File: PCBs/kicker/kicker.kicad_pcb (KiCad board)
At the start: 2 copper layers, 11 parts, among them Q1 CSD19534Q5A

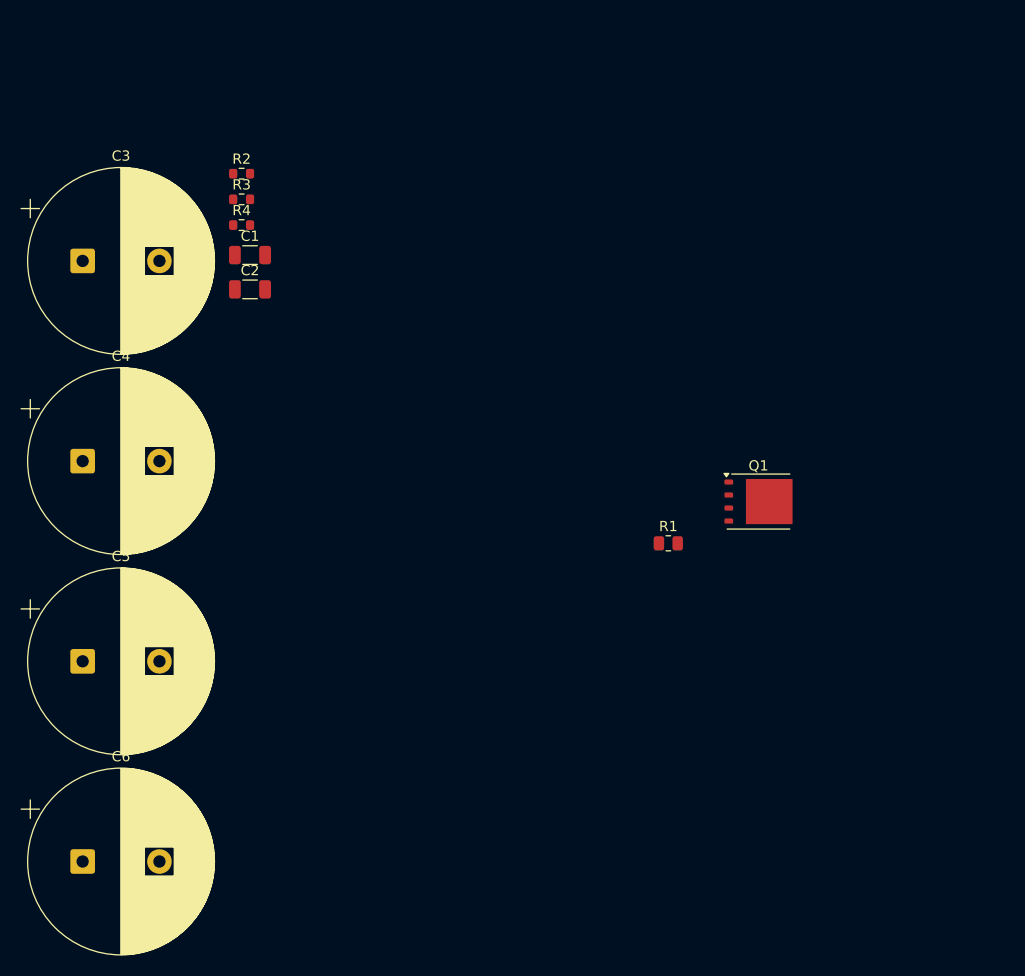
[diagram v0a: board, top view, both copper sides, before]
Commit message: fix driver footprint
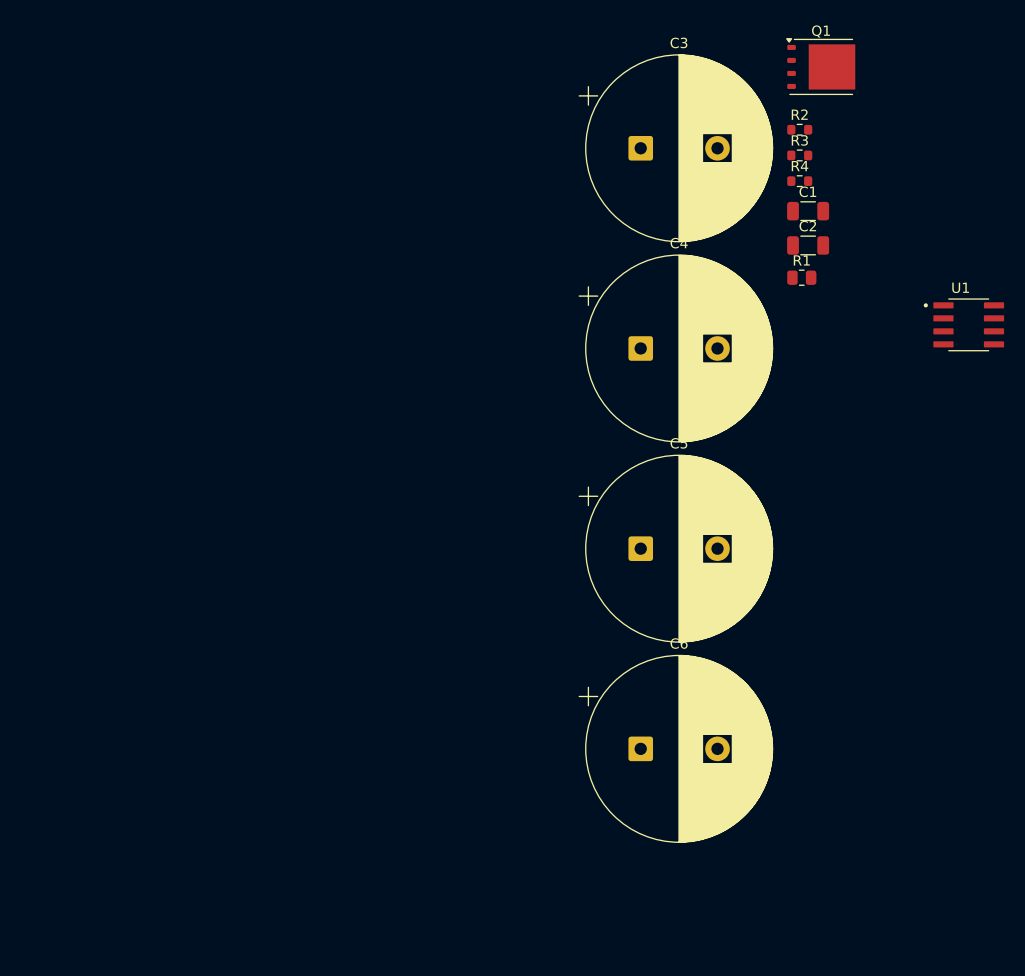
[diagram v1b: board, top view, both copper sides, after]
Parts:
- added U1: UCC27624DR, Footprints:SOIC127P599X175-8N, F.Cu at (169.5, 76.1)
- moved C3 55.6 mm to (137.5, 58.9)
- moved C4 55.6 mm to (137.5, 78.4)
- moved C5 55.6 mm to (137.5, 98.0)
- moved C6 55.6 mm to (137.5, 117.5)
- moved R2 54.7 mm to (153.0, 57.0)
- moved R3 54.7 mm to (153.0, 59.5)
- moved R4 54.7 mm to (153.0, 62.1)
- moved C1 54.7 mm to (153.8, 65.0)
- moved C2 54.7 mm to (153.8, 68.3)
- moved Q1 42.9 mm to (155.1, 50.9)
- moved R1 29.0 mm to (153.2, 71.5)

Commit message: kicker v0.1
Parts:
- added J1: Conn_01x02_Socket, Connector_JST:JST_XH_S2B-XH-A-1_1x02_P2.50mm_Horizontal, F.Cu at (168.8, 66.3)
- added J2: Conn_01x04_Socket, Connector_JST:JST_XH_S4B-XH-A-1_1x04_P2.50mm_Horizontal, F.Cu at (123.0, 63.5)
- added J3: Conn_01x01_Socket, Connector_Wire:SolderWirePad_1x01_SMD_5x10mm, F.Cu at (138.4, 126.0)
- added J4: Conn_01x01_Socket, Connector_Wire:SolderWirePad_1x01_SMD_5x10mm, F.Cu at (145.0, 126.0)
- added Q2: IRF540N, Package_TO_SOT_THT:TO-220-3_Horizontal_TabDown, F.Cu at (162.3, 123.0)
- added R5: 100, Package_TO_SOT_SMD:TO-263-2, F.Cu at (180.3, 63.9)
- added R6: 10k, Resistor_SMD:R_0603_1608Metric, F.Cu at (95.7, 128.0)
- added R7: 100, Resistor_SMD:R_0603_1608Metric, F.Cu at (95.7, 130.0)
- added R8: 2, Resistor_SMD:R_0805_2012Metric, F.Cu at (110.1, 128.5)
- added R9: 10k, Resistor_SMD:R_0603_1608Metric, F.Cu at (162.2, 120.0)
- moved R2 89.3 mm to (95.7, 125.5), turned to 180 degrees
- moved C1 86.0 mm to (102.5, 134.0), turned to 180 degrees
- moved Q1 84.7 mm to (117.0, 126.5)
- moved R4 84.0 mm to (95.7, 123.5), turned to 180 degrees
- moved U1 83.9 mm to (102.5, 126.5)
- moved R3 83.5 mm to (114.2, 133.5)
- moved C2 81.0 mm to (102.5, 131.0), turned to 180 degrees
- moved R1 69.5 mm to (110.1, 126.0)
- moved C4 33.3 mm to (117.5, 105.0)
- moved C3 31.7 mm to (117.5, 83.5)
- moved C5 31.5 mm to (165.5, 83.5)
- moved C6 31.3 mm to (166.0, 104.5)
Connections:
- C3 pad 1: unconnected-(C3-Pad1) -> Net-(C3-Pad1)
- C3 pad 2: unconnected-(C3-Pad2) -> /SOLin
- C4 pad 1: unconnected-(C4-Pad1) -> Net-(C3-Pad1)
- C4 pad 2: unconnected-(C4-Pad2) -> /SOLin
- C5 pad 1: unconnected-(C5-Pad1) -> Net-(C3-Pad1)
- C5 pad 2: unconnected-(C5-Pad2) -> /SOLin
- C6 pad 1: unconnected-(C6-Pad1) -> Net-(C3-Pad1)
- C6 pad 2: unconnected-(C6-Pad2) -> /SOLin
- U1 pad 4: GND -> Net-(U1-INB)
- U1 pad 5: unconnected-(U1-OUTB-Pad5) -> Net-(U1-OUTB)
- U1 pad 8: GND -> VCC
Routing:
- net VCC: track 0.00 -> 1.62 mm
- net GND: track 0.00 -> 1.14 mm

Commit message: ee
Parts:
- added C10: 220u, Capacitor_SMD:CP_Elec_10x10.5, F.Cu at (259.0, 35.5)
- added C7: 1u, Capacitor_SMD:C_1206_3216Metric, F.Cu at (232.0, 50.0)
- added C8: 220u, Capacitor_SMD:CP_Elec_10x10.5, F.Cu at (227.5, 35.5)
- added C9: 1u, Capacitor_SMD:C_1206_3216Metric, F.Cu at (266.5, 43.0)
- added D1: B560C, digikey-footprints:DO-214AB, F.Cu at (258.9, 48.0)
- added D2: SS210, Diode_SMD:D_SMA, F.Cu at (268.5, 48.0)
- added L1: 47u, Inductor_SMD:L_Sunlord_MWSA1206S-470, F.Cu at (243.5, 35.0)
- added R10: 10k, Resistor_SMD:R_0603_1608Metric, F.Cu at (138.3, 48.4)
- added R11: 47k, Resistor_SMD:R_0603_1608Metric, F.Cu at (251.0, 57.5)
- added R12: 2k, Resistor_SMD:R_0603_1608Metric, F.Cu at (236.0, 57.5)
- added RV1: 50k, Potentiometer_THT:Potentiometer_Bourns_3296W_Vertical, F.Cu at (246.0, 57.5)
- added U2: XL6019E1, Package_TO_SOT_SMD:TO-263-5_TabPin3, F.Cu at (245.6, 48.2)
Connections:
- net /mcuDrive renamed /mcuKick
- C3 pad 2: /SOLin -> GND
- C4 pad 2: /SOLin -> GND
- C5 pad 2: /SOLin -> GND
- C6 pad 2: /SOLin -> GND
- J4 pad 1: /SOLin -> GND
- R8 pad 2: /outCAP -> /capEN
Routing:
- added copper zone on B.Cu, net GND
- added copper zone on F.Cu, net Net-(D1-A)
- added copper zone on F.Cu, net Net-(D1-K)

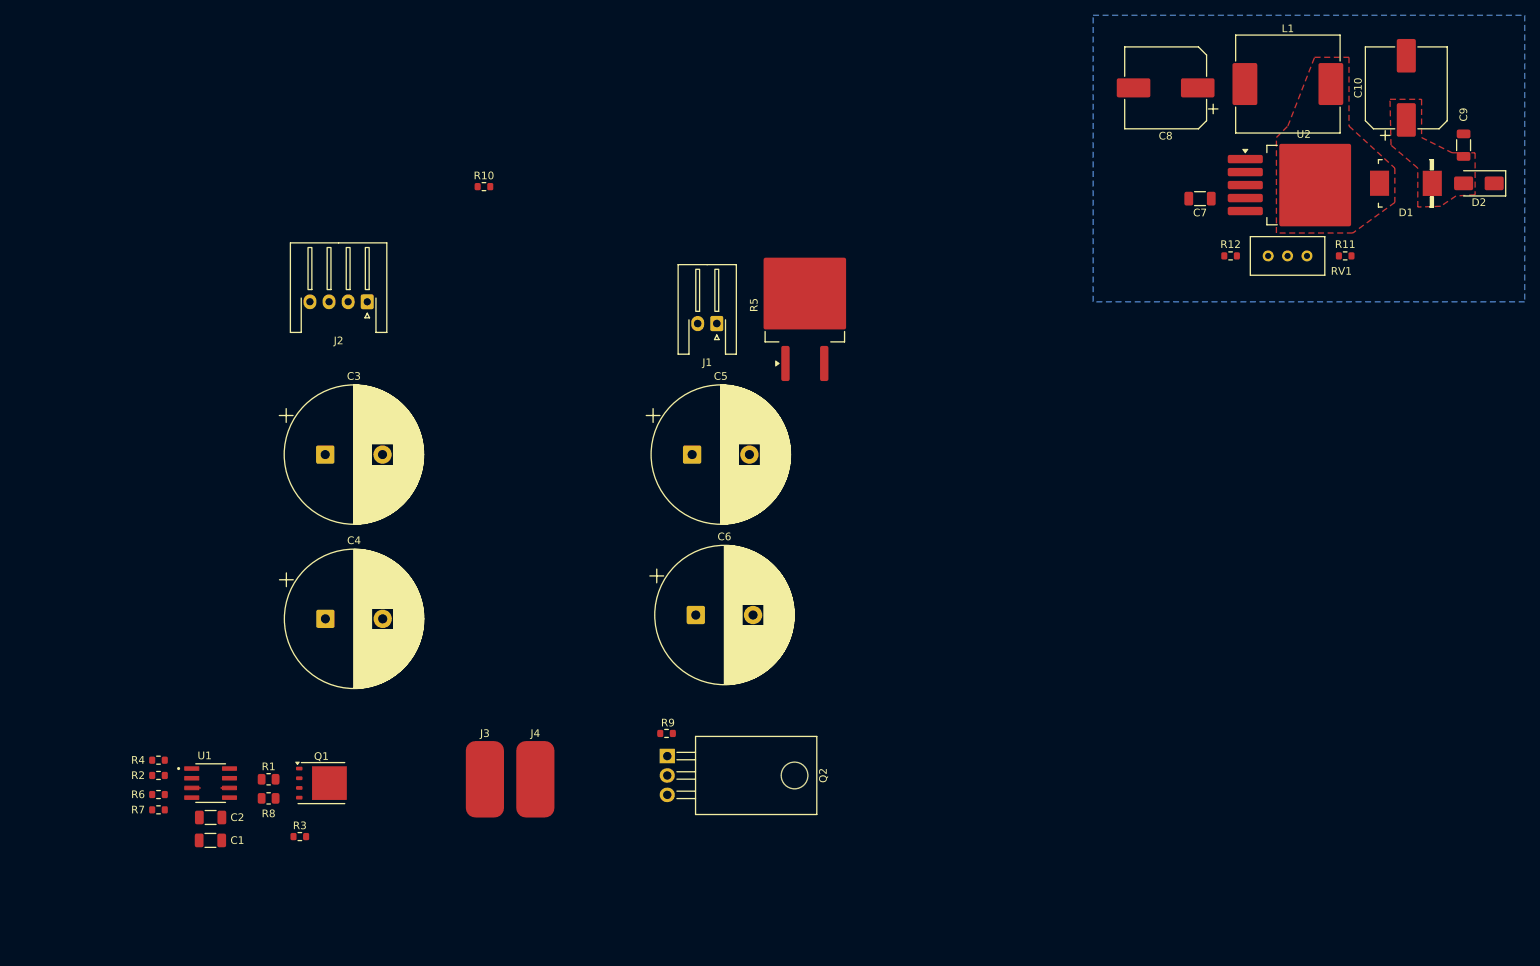
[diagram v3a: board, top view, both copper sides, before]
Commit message: kicker board and outline
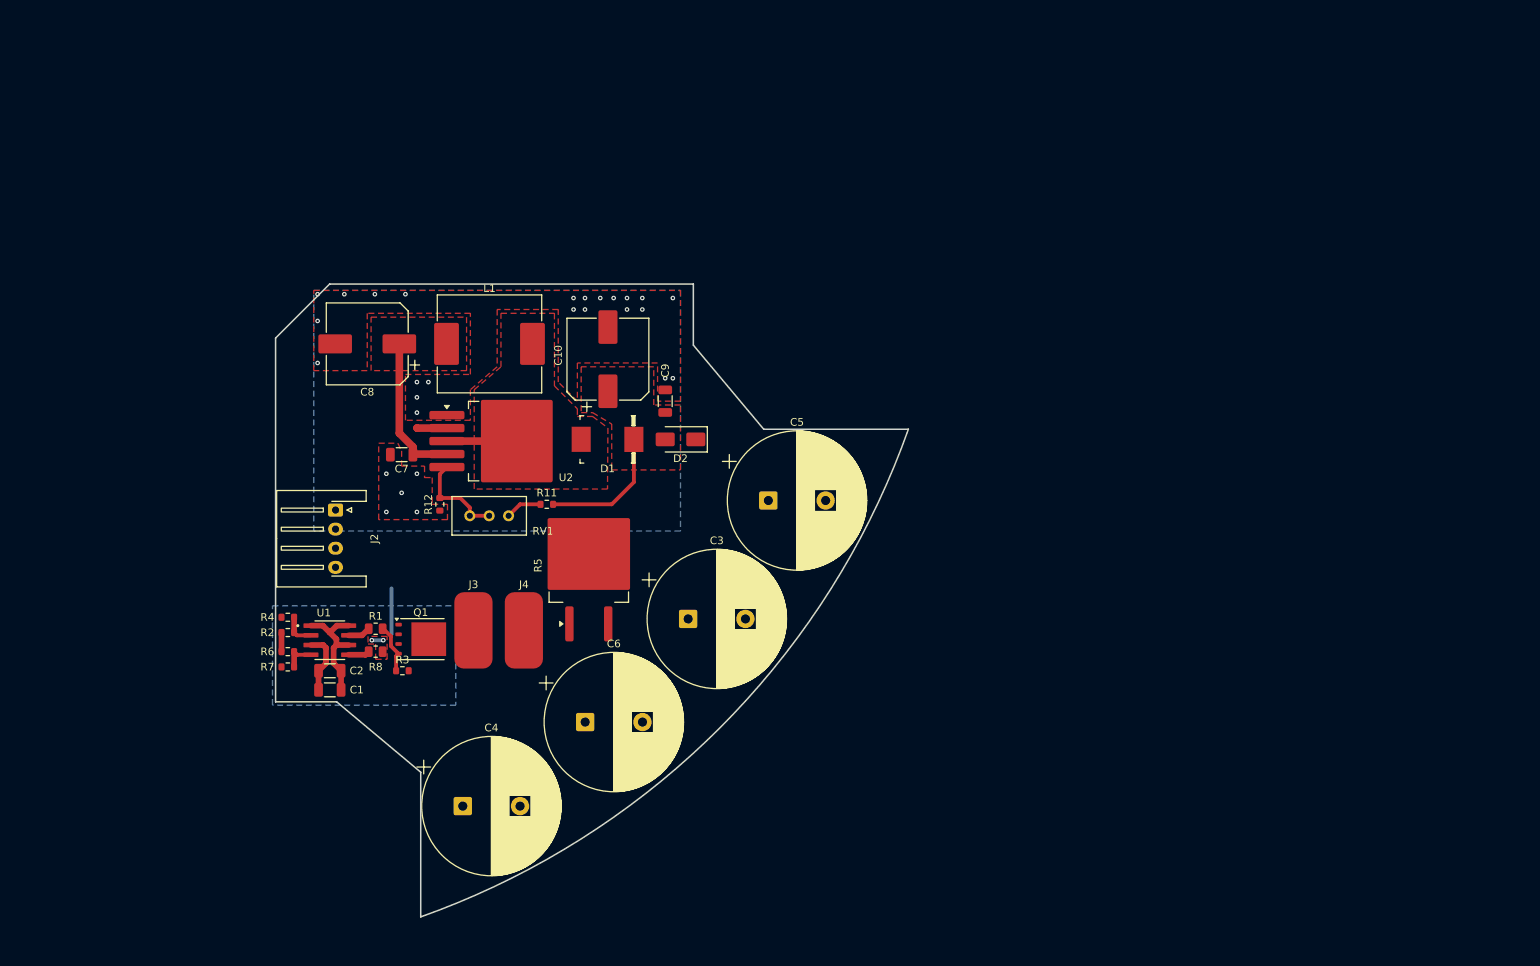
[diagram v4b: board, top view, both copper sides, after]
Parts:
- removed J1: Conn_01x02_Socket, Connector_JST:JST_XH_S2B-XH-A-1_1x02_P2.50mm_Horizontal
- removed Q2: IRF540N, Package_TO_SOT_THT:TO-220-3_Horizontal_TabDown
- removed R10, R9: 10k, Resistor_SMD:R_0603_1608Metric
- moved C10 110.4 mm to (154.5, 71.0)
- moved RV1 109.9 mm to (141.5, 91.5)
- moved L1 109.9 mm to (139.0, 69.0)
- moved C7 109.7 mm to (127.5, 83.5)
- moved C8 109.7 mm to (123.0, 69.0)
- moved C9 109.7 mm to (162.0, 76.5)
- moved D1 109.7 mm to (154.4, 81.5)
- moved D2 109.7 mm to (164.0, 81.5)
- moved U2 109.7 mm to (141.1, 81.7)
- moved R11 109.4 mm to (146.5, 90.0)
- moved R12 108.5 mm to (132.5, 90.0), turned to -90 degrees
- moved C3 52.1 mm to (165.0, 105.0)
- moved R5 44.3 mm to (152.0, 98.0)
- moved C4 30.4 mm to (135.5, 129.5)
- moved J2 27.6 mm to (118.8, 90.8), turned to -90 degrees
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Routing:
- net VCC: track 1.62 -> 35.4 mm
- net Net-(D1-K): track 0.00 -> 17.4 mm
- net Net-(U2-FB): track 0.00 -> 12.5 mm
- net /capEN: track 0.00 -> 11.4 mm, vias 0 -> 2
- net GND: track 1.14 -> 10.5 mm, vias 0 -> 28
- net Net-(D1-A): track 0.00 -> 9.15 mm
- net /outFET: track 0.00 -> 6.55 mm
- net Net-(R11-Pad2): track 0.00 -> 4.80 mm
- net Net-(U1-INB): track 0.13 -> 4.51 mm
- net Net-(U1-INA): track 0.19 -> 4.36 mm
- net Net-(U1-OUTA): track 0.00 -> 2.98 mm
- net Net-(U1-OUTB): track 0.00 -> 2.79 mm
- added copper zone on F.Cu, net /capEN
- added copper zone on F.Cu, net GND
- added copper zone on F.Cu, net VCC
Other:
- board outline added: 82.8 x 82.8 mm

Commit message: kicker V1
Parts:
- added ?: , , F.Cu at (189.6, 83.2)
- added ?: , , F.Cu at (162.7, 64.2)
- added ?: , , F.Cu at (133.0, 139.8)
- added R9: 3k, Resistor_SMD:R_2512_6332Metric, F.Cu at (143.0, 110.5)
- added REF**: MountingHole_3.2mm_M3_DIN965_Pad, MountingHole:MountingHole_3.2mm_M3_DIN965_Pad, F.Cu at (114.0, 112.9)
- added TP1: 48V probe, TestPoint:TestPoint_THTPad_1.5x1.5mm_Drill0.7mm, F.Cu at (166.0, 91.5)
- added TP2: GND probe, TestPoint:TestPoint_THTPad_1.5x1.5mm_Drill0.7mm, F.Cu at (114.5, 74.5)
- J2: footprint Connector_JST:JST_XH_S4B-XH-A-1_1x04_P2.50mm_Horizontal -> Connector_JST:JST_XH_B4B-XH-A_1x04_P2.50mm_Vertical
- U1: footprint Footprints:SOIC127P599X175-8N -> Package_SO:SOIC-8_3.9x4.9mm_P1.27mm
- moved J4 16.8 mm to (129.0, 115.0)
- moved R1 8.61 mm to (129.6, 99.6)
- moved R3 8.61 mm to (133.1, 105.1)
- moved R8 8.61 mm to (129.6, 102.6)
- moved C1 8.61 mm to (123.5, 107.6)
- moved C2 8.61 mm to (123.5, 105.1)
- moved R2 8.61 mm to (118.0, 100.1)
- moved R4 8.61 mm to (118.0, 98.1)
- moved R6 8.61 mm to (118.0, 102.6)
- moved R7 8.61 mm to (118.0, 104.6)
- moved U1 8.61 mm to (123.5, 101.1)
- moved Q1 8.61 mm to (135.4, 101.0)
- moved J3 6.64 mm to (135.5, 113.0)
- moved J2 3.26 mm to (116.5, 88.5), turned to 90 degrees
- moved R5 3.03 mm to (152.5, 101.0), turned to 0 degrees
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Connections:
- C3 pad 1: Net-(C3-Pad1) -> /SOLin
- C4 pad 1: Net-(C3-Pad1) -> /SOLin
- C5 pad 1: Net-(C3-Pad1) -> /SOLin
- C6 pad 1: Net-(C3-Pad1) -> /SOLin
- J4 pad 1: GND -> /SOLin
- R5 pad 2: Net-(C3-Pad1) -> /SOLin
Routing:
- net /SOLin: track 0.00 -> 98.3 mm
- net /48V+: track 0.00 -> 37.1 mm
- net VCC: track 35.4 -> 67.3 mm
- net /capEN: track 11.4 -> 37.6 mm, vias 2 -> 4
- net /mcuCap: track 0.00 -> 17.7 mm
- net /mcuKick: track 0.00 -> 14.5 mm
- net /SOLout: track 0.00 -> 12.4 mm
- net GND: track 10.5 -> 13.1 mm, vias 28 -> 70
- added copper zone on F.Cu, net /SOLin
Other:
- board size 82.8 x 82.8 mm -> 81.5 x 81.6 mm
- board text added: "48V"
- board text added: "GND"
